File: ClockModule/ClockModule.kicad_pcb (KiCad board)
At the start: 2 copper layers, 93.5 x 65.5 mm, 34 parts, among them J1 Conn_01x05_Pin, SW1 SW_SPDT, U1 LM555xN, U2 LM555xN, U3 OR, U4 NOT, U6 LM555xN

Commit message: Final clock updates
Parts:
- D1, D2, D3: footprint LED_THT:LED_D2.0mm_W4.8mm_H2.5mm_FlatTop -> LED_THT:LED_D5.0mm
- J1: footprint Connector_PinHeader_1.00mm:PinHeader_1x05_P1.00mm_Horizontal -> Connector_PinHeader_2.54mm:PinHeader_1x05_P2.54mm_Vertical
- moved R3 13.7 mm to (77.5, 102.8), turned to 180 degrees
- moved R6 13.1 mm to (100.7, 103.5), turned to 180 degrees
- moved D3 10.3 mm to (133.0, 96.5)
- moved D1 10.0 mm to (82.0, 105.8)
- moved SW1 9.90 mm to (120.1, 85.5)
- moved REF** 9.55 mm to (136.2, 74.2)
- moved R7 9.39 mm to (131.5, 93.0)
- moved D2 9.25 mm to (105.2, 105.8)
- moved REF** 9.20 mm to (136.2, 120.8)
- moved S1 8.80 mm to (97.2, 85.0)
- moved REF** 8.55 mm to (60.8, 74.2)
- moved C7 8.23 mm to (126.9, 100.2)
- moved C8 8.23 mm to (126.9, 92.2)
- moved REF** 8.16 mm to (60.8, 120.8)
- moved C2 7.91 mm to (68.5, 92.5)
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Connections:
- J1 pad 1: GND -> +5V
- J1 pad 2: +5V -> GND
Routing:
- net /AstableClock/CLK: track 57.7 -> 47.3 mm
- net Net-(SW1-A): track 18.9 -> 13.0 mm
- net /ClockSelect/BistableDebouncingCircuit/Select: track 51.5 -> 46.2 mm
- net /ClockSelect/Manual_clk: track 41.0 -> 35.7 mm
- net Net-(U2-TR): track 17.5 -> 12.4 mm
- net /~{clk}: track 44.8 -> 40.3 mm
- net Net-(SW1-C): track 22.3 -> 19.0 mm
- net Net-(U6-CV): track 9.83 -> 6.60 mm
- net Net-(D2-K): track 8.37 -> 5.47 mm
- net Net-(D3-K): track 7.00 -> 4.12 mm
- net Net-(U1-DIS): track 21.8 -> 19.0 mm
- net Net-(U1-THR): track 27.2 -> 24.6 mm
- net Net-(D1-K): track 8.22 -> 5.74 mm
- net Net-(U1-CV): track 5.46 -> 3.18 mm
- net /halt: track 50.7 -> 48.5 mm
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- added copper zone on F.Cu, net +5V
- added copper zone on B.Cu, net GND
- removed copper zone on B.Cu, net +5V
- removed copper zone on F.Cu, net GND
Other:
- board size 93.5 x 65.5 mm -> 81.5 x 52.5 mm
- board text added: "Clock"
- board text added: "Halt"
- board text added: "VCC"
- board text added: "~{CLK}"
- board text removed: "+5V"
- board text removed: "HALT"
- board text removed: "TODO: Double check 4xAND footprint"
- board text removed: "TODO: Figure out if I need more clock pins 1 for each module? Or just add it to the bus module and pass it around there?"
- board text removed: "~CLK"

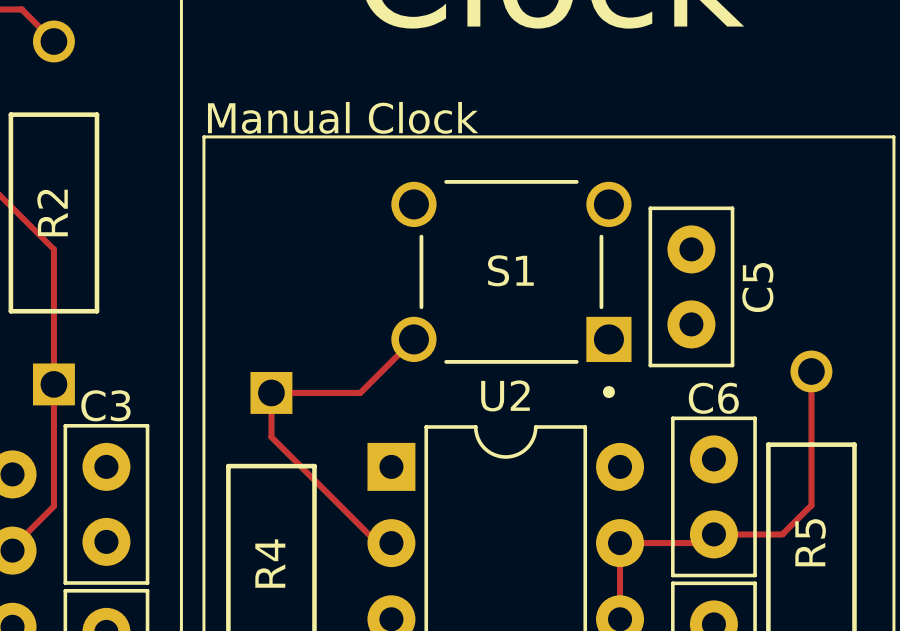
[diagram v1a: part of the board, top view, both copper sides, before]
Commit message: Fixed push button always shorting
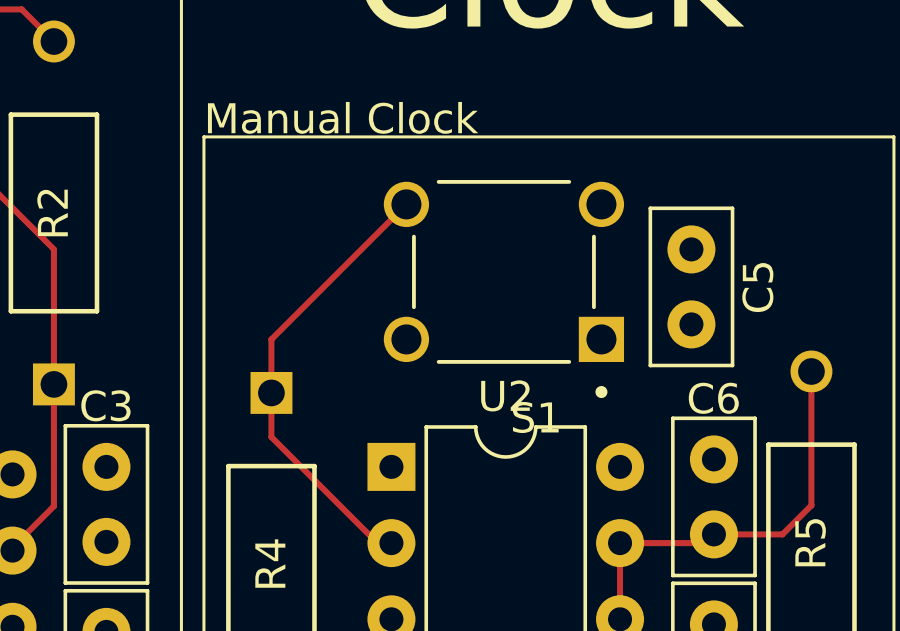
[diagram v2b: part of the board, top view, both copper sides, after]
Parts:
- S1: value B3U-1000P -> TactileSwitch
- moved S1 0.25 mm to (97.0, 85.0)
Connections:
- S1 pad 2: Net-(U2-TR) -> (no net)
- S1 pad 4: (no net) -> Net-(U2-TR)
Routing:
- net Net-(U2-TR): track 12.4 -> 15.1 mm

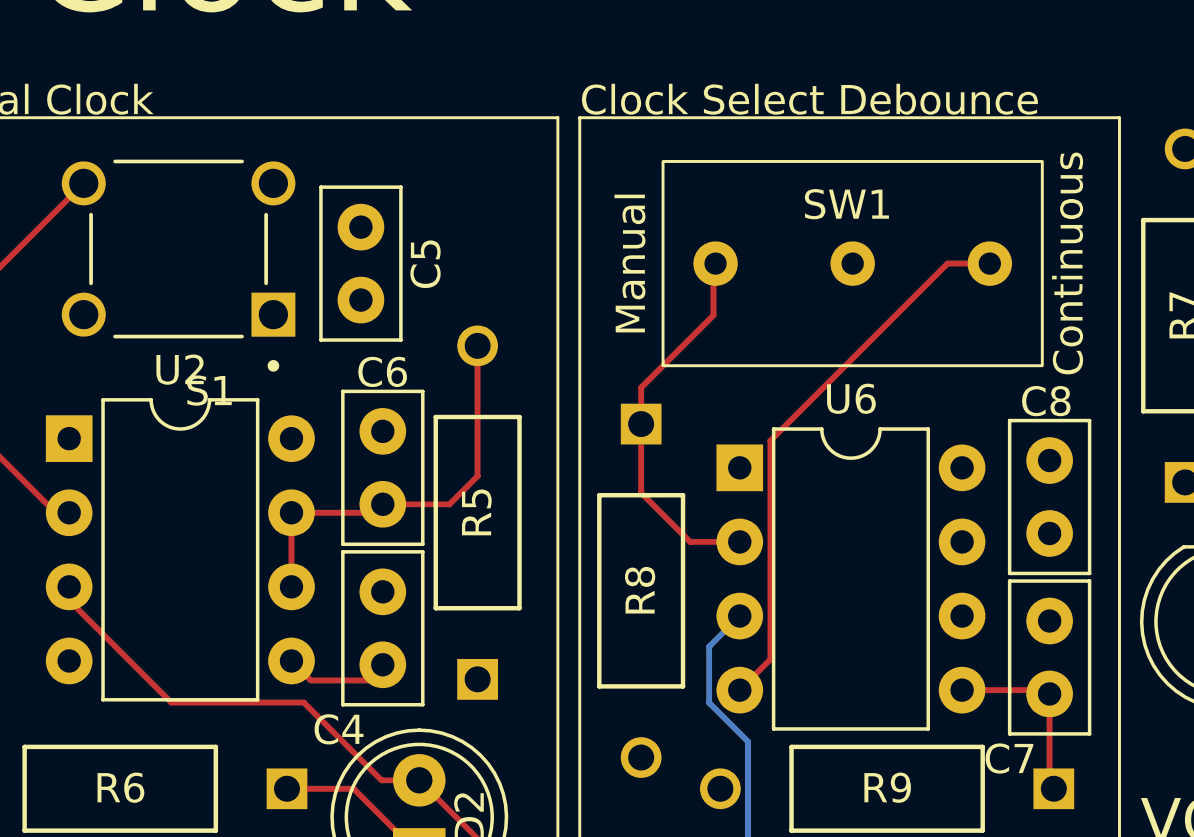
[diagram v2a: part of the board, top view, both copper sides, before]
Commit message: Fixed double throw switch footprint
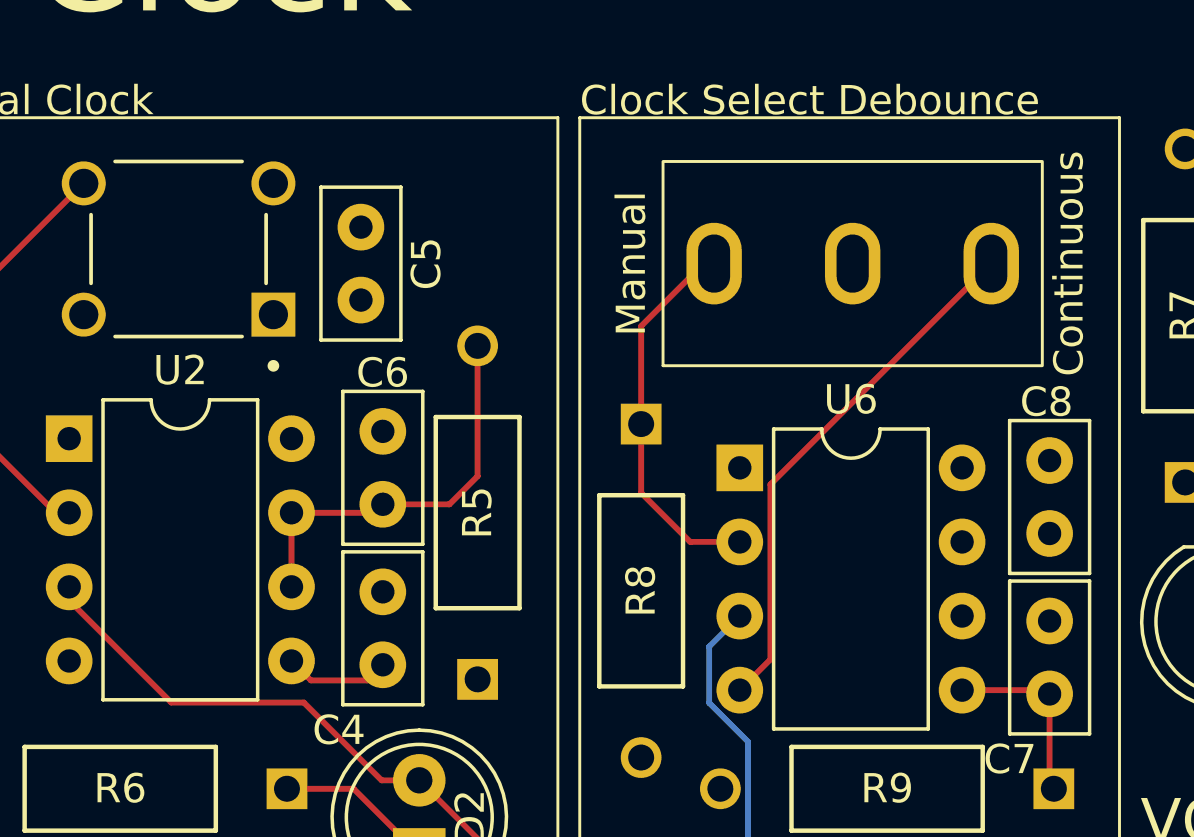
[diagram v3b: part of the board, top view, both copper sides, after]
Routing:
- net Net-(SW1-C): track 19.0 -> 18.2 mm
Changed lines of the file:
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@@
 			(unlocked yes)
 			(layer "F.SilkS")
+			(hide yes)
 			(effects
 				(font
@@
 			)
 		)
-		(pad "1" thru_hole circle
-			(at 0 -4.7 90)
-			(size 1.524 1.524)
-			(drill 0.762)
+		(pad "1" thru_hole oval
+			(at 0 -4.75 180)
+			(size 1.9 2.8)
+			(drill oval 1.1 2)
 			(layers "*.Cu" "*.Mask")
 			(remove_unused_layers no)
@@
 			(pintype "passive")
 		)
-		(pad "2" thru_hole circle
-			(at 0 0 90)
-			(size 1.524 1.524)
-			(drill 0.762)
+		(pad "2" thru_hole oval
+			(at 0 0 180)
+			(size 1.9 2.8)
+			(drill oval 1.1 2)
 			(layers "*.Cu" "*.Mask")
 			(remove_unused_layers no)
@@
 			(pintype "passive")
 		)
-		(pad "3" thru_hole circle
-			(at 0 4.7 90)
-			(size 1.524 1.524)
-			(drill 0.762)
+		(pad "3" thru_hole oval
+			(at 0 4.75 180)
+			(size 1.9 2.8)
+			(drill oval 1.1 2)
 			(layers "*.Cu" "*.Mask")
 			(remove_unused_layers no)
@@
 		(at 97 85 180)
 		(property "Reference" "S1"
-			(at -1.079 -4.889 360)
+			(at 0.25 0.25 360)
 			(layer "F.SilkS")
+			(hide yes)
 			(effects
 				(font
@@
 	)
 	(segment
-		(start 114.54 95.04)
-		(end 116.235 95.04)
-		(width 0.2)
-		(layer "F.Cu")
-		(net 21)
-	)
-	(segment
-		(start 115.335 87.27)
-		(end 112.855 89.75)
+		(start 115 85.5)
+		(end 112.855 87.645)
 		(width 0.2)
 		(layer "F.Cu")
@@
 	)
 	(segment
-		(start 112.855 89.75)
+		(start 112.855 87.645)
 		(end 112.855 91)
 		(width 0.2)
@@
 	)
 	(segment
-		(start 112.855 91)
-		(end 112.855 93.355)
+		(start 115.355 85.5)
+		(end 115 85.5)
 		(width 0.2)
 		(layer "F.Cu")
@@
 	)
 	(segment
-		(start 115.335 85.57)
-		(end 115.335 87.27)
+		(start 114.54 95.04)
+		(end 116.235 95.04)
 		(width 0.2)
 		(layer "F.Cu")
@@
 	)
 	(segment
-		(start 115.405 85.5)
-		(end 115.335 85.57)
+		(start 112.855 91)
+		(end 112.855 93.355)
 		(width 0.2)
 		(layer "F.Cu")
@@
 	(segment
 		(start 124.805 85.5)
-		(end 123.355 85.5)
+		(end 124.855 85.5)
 		(width 0.2)
 		(layer "F.Cu")
@@
 	)
 	(segment
-		(start 117.285 99.07)
-		(end 116.235 100.12)
+		(start 117.285 93.07)
+		(end 117.285 99.07)
 		(width 0.2)
 		(layer "F.Cu")
@@
 	)
 	(segment
-		(start 117.285 91.57)
-		(end 117.285 99.07)
+		(start 117.285 99.07)
+		(end 116.235 100.12)
 		(width 0.2)
 		(layer "F.Cu")
@@
 	)
 	(segment
-		(start 123.355 85.5)
-		(end 117.285 91.57)
+		(start 124.855 85.5)
+		(end 117.285 93.07)
 		(width 0.2)
 		(layer "F.Cu")

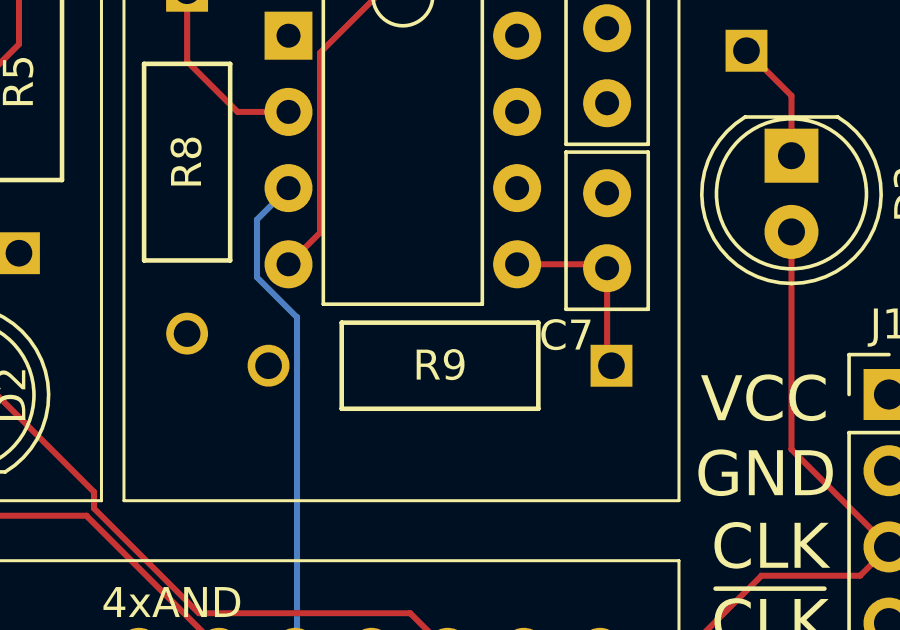
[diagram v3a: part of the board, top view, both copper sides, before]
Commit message: Switch pull up resistor was connected to wrong pin. Connected to switch now
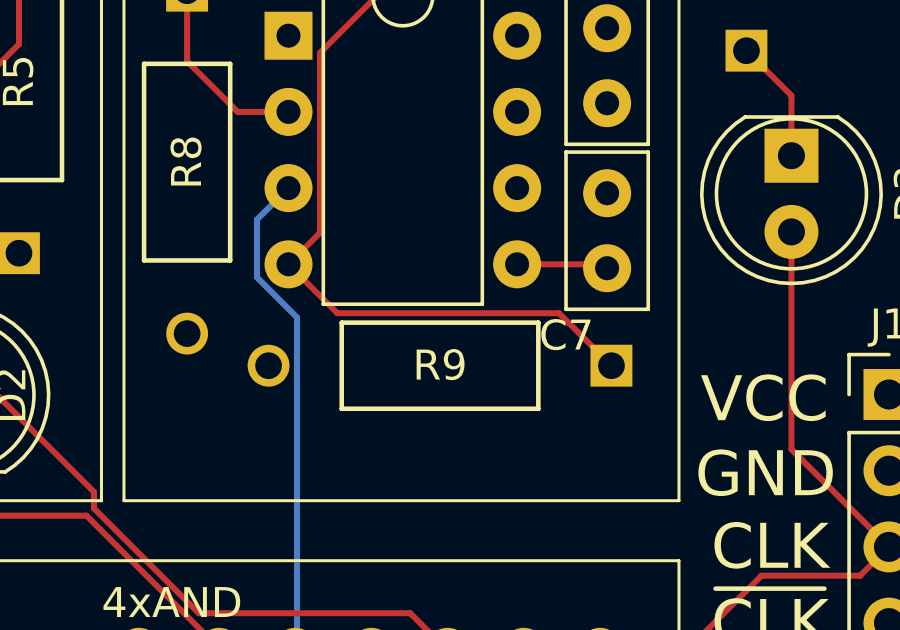
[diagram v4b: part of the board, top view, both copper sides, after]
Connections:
- R9 pad 1: Net-(U6-CV) -> Net-(SW1-C)
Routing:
- net Net-(SW1-C): track 18.2 -> 30.4 mm
- net Net-(U6-CV): track 6.60 -> 3.29 mm
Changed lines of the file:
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@@
 			(layers "*.Cu" "*.Mask")
 			(remove_unused_layers no)
-			(net 20 "Net-(U6-CV)")
+			(net 22 "Net-(SW1-C)")
 			(pintype "passive")
 		)
@@
 		(at 97 85 180)
 		(property "Reference" "S1"
-			(at 0.25 0.25 360)
+			(at 0.25 0.25 0)
 			(layer "F.SilkS")
 			(hide yes)
@@
 		)
 		(property "Value" "TactileSwitch"
-			(at 12.256 4.889 360)
+			(at 12.256 4.889 0)
 			(layer "F.Fab")
 			(effects
@@
 		)
 		(property "Footprint" "_DownloadFootprints:tactile_switch"
-			(at 0 0 360)
+			(at 0 0 0)
 			(layer "F.Fab")
 			(hide yes)
@@
 		)
 		(property "Datasheet" "https://omronfs.omron.com/en_US/ecb/products/pdf/en-b3u.pdf"
-			(at 0 0 360)
+			(at 0 0 0)
 			(layer "F.Fab")
 			(hide yes)
@@
 		)
 		(property "Description" "SWITCH TACTILE SPST-NO 0.05A 12V"
-			(at 0 0 360)
+			(at 0 0 0)
 			(layer "F.Fab")
 			(hide yes)
@@
 	)
 	(segment
-		(start 126.855 103.355)
-		(end 126.855 100.25)
-		(width 0.2)
-		(layer "F.Cu")
-		(net 20)
-	)
-	(segment
-		(start 127 103.5)
-		(end 126.855 103.355)
-		(width 0.2)
-		(layer "F.Cu")
-		(net 20)
-	)
-	(segment
 		(start 123.855 100.12)
 		(end 123.855 100.355)
@@
 	)
 	(segment
+		(start 117.865 101.75)
+		(end 116.235 100.12)
+		(width 0.2)
+		(layer "F.Cu")
+		(net 22)
+	)
+	(segment
 		(start 117.285 93.07)
 		(end 117.285 99.07)
@@
 	)
 	(segment
+		(start 125.25 101.75)
+		(end 117.865 101.75)
+		(width 0.2)
+		(layer "F.Cu")
+		(net 22)
+	)
+	(segment
 		(start 124.855 85.5)
 		(end 117.285 93.07)
 		(width 0.2)
 		(layer "F.Cu")
+		(net 22)
+	)
+	(segment
+		(start 127 103.5)
+		(end 125.25 101.75)
+		(width 0.2)
+		(layer "F.Cu")
